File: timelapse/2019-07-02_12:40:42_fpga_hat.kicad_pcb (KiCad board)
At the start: 4 copper layers, 65 x 56.5 mm, 90 parts, among them J1 2x20, J2 AudioJack3, J3 Conn_02x06_Top_Bottom, J4 Conn_02x06_Top_Bottom, J5 Conn_02x06_Top_Bottom, J6 Conn_01x02, SW1 PTS815, SW2 PTS815, SW3 PTS815, SW4 PTS815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

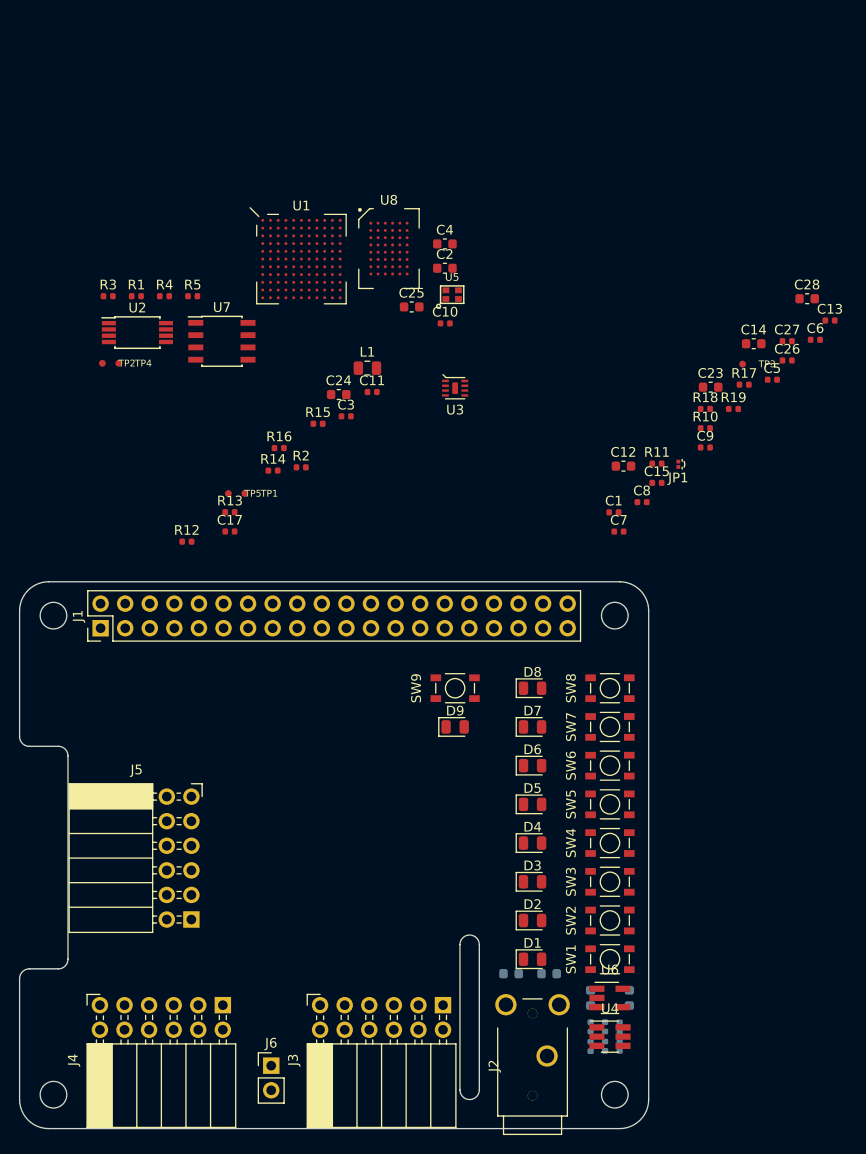
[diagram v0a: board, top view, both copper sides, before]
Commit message: Start placing components
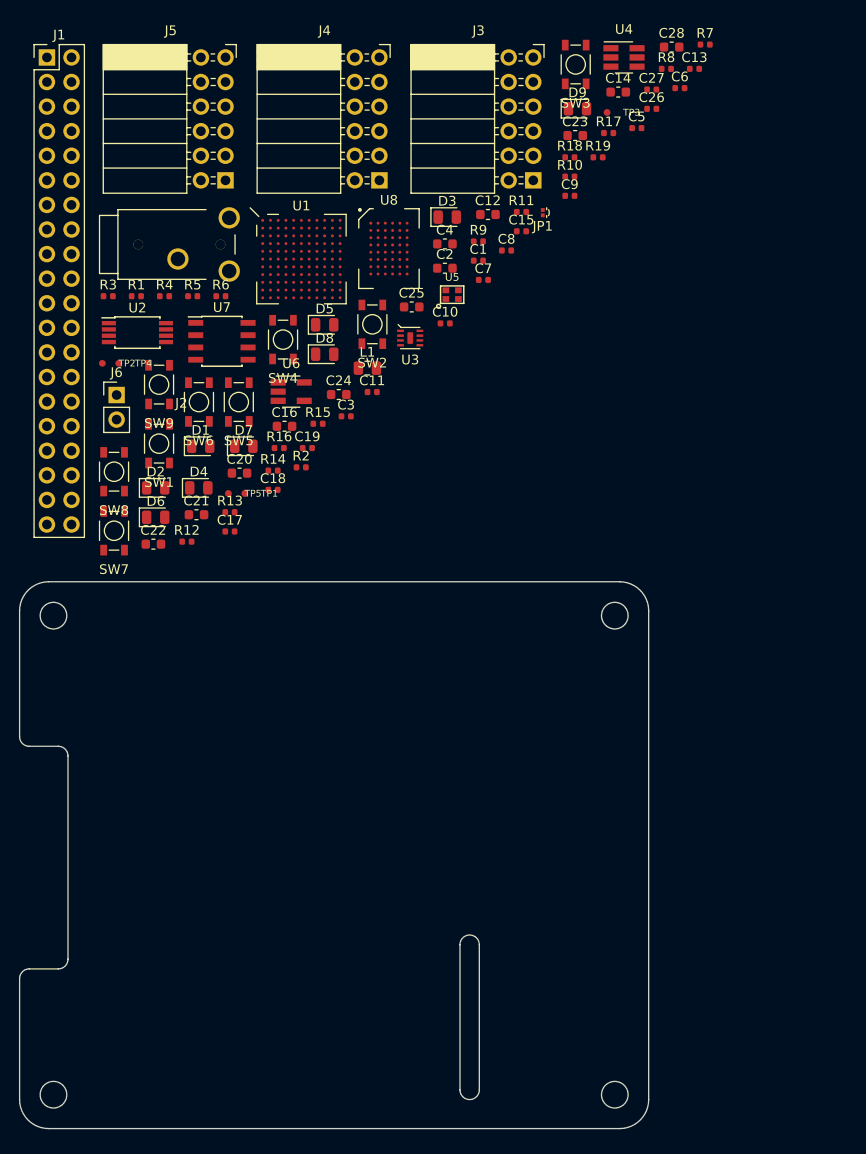
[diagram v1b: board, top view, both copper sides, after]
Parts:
- C16, C18, C19, C20, C21, C22, R6, R7, R8, R9: moved to F.Cu
- moved R7 103.9 mm to (170.8, 24.5), turned to 0 degrees
- moved U4 101.2 mm to (162.4, 25.8)
- moved R8 99.2 mm to (166.8, 27.0), turned to 0 degrees
- moved J2 91.5 mm to (116.4, 45.1), turned to 0 degrees
- moved J4 86.7 mm to (137.2, 38.5), turned to 0 degrees
- moved R6 86.0 mm to (120.8, 50.5), turned to 0 degrees
- moved J3 85.7 mm to (153.1, 38.5), turned to 0 degrees
- moved SW3 84.5 mm to (157.5, 26.6), turned to 0 degrees
- moved R9 84.2 mm to (147.4, 44.8), turned to 0 degrees
- moved J5 76.5 mm to (121.3, 38.5)
- moved J6 71.1 mm to (110.0, 60.7)
- moved U6 70.8 mm to (128.1, 60.4)
- moved SW1 70.8 mm to (114.4, 65.7), turned to 0 degrees
- moved D3 69.2 mm to (144.2, 42.3)
- moved C19 68.4 mm to (129.7, 66.2), turned to 0 degrees
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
